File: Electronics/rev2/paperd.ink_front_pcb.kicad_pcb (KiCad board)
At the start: 4 copper layers, 92.1 x 8 mm, 4 parts, among them J2 Conn_01x14

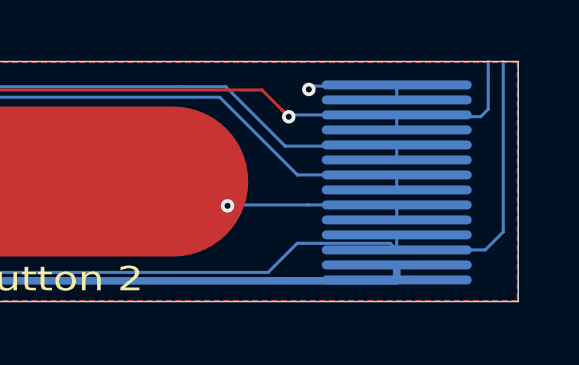
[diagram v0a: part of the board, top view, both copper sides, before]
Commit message: split PCB into main and front
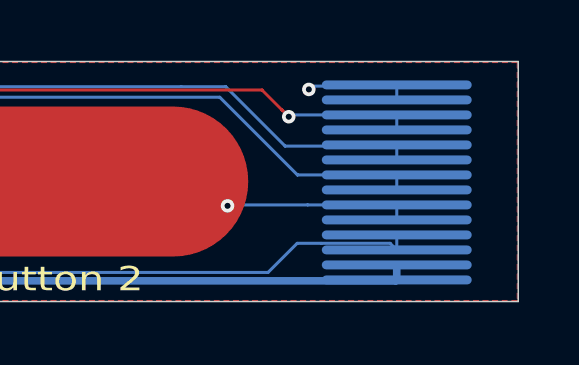
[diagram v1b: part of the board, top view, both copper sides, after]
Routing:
- net ~FPC_LED_R: track 52.7 -> 43.2 mm
- net ~FPC_LED_B: track 54.1 -> 49.4 mm
- net UART_TXD0: track 2.18 -> 0.00 mm
- net UART_RXD0: track 1.58 -> 0.00 mm
- removed copper zone on In1.Cu, net +3V3
- removed copper zone on In2.Cu, net GND
